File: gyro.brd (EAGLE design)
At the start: 14 x 15.2 mm, 9 parts, among them IC2 LGD20H

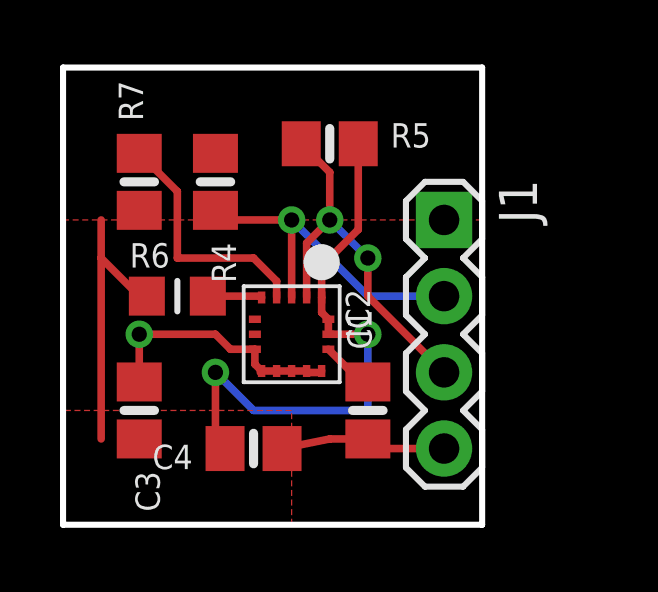
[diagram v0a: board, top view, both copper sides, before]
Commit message: boards rounted with silk screen
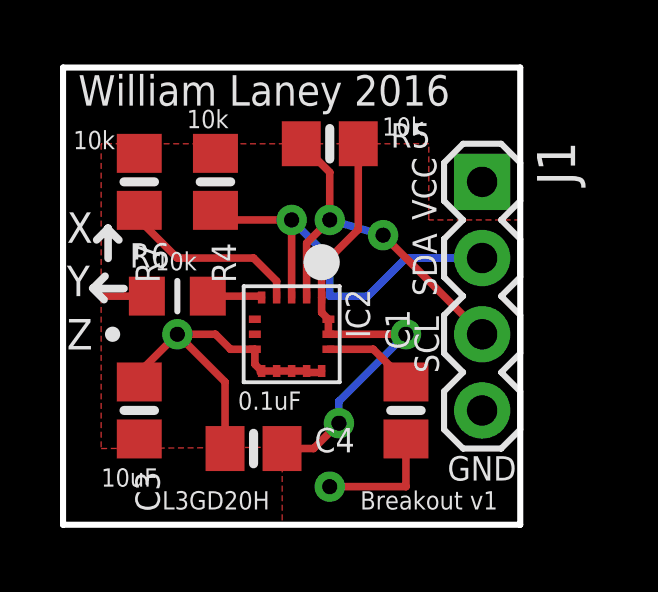
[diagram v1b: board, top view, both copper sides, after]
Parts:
- moved J1 1.80 mm to (14.0, 11.4)
- moved C1 1.27 mm to (11.4, 3.81)
- turned C4 to 0 degrees
- turned R7 to 270 degrees
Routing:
- net +3V3: track 28.4 -> 17.4 mm
- net SDA: track 11.4 -> 13.9 mm
- net GND: track 14.1 -> 16.4 mm, vias 1 -> 2
- net SDO/SAO: track 8.19 -> 6.29 mm
- net N$3: track 1.77 -> 3.04 mm
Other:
- board size 14 x 15.2 mm -> 15.2 x 15.2 mm
- board text added: "0.1uF"
- board text added: "10k"
- board text added: "10uF"
- board text added: "Breakout v1"
- board text added: "GND"
- board text added: "L3GD20H"
- board text added: "SCL"
- board text added: "SDA"
- board text added: "VCC"
- board text added: "William Laney 2016"
- board text added: "X"
- board text added: "Y"
- board text added: "Z"

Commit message: shortedn connections, removed via
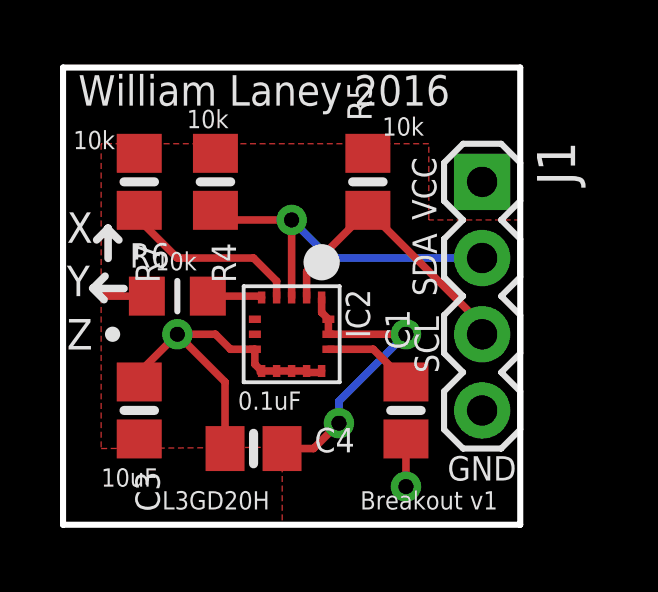
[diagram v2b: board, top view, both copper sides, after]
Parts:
- moved R5 1.80 mm to (10.2, 11.4), turned to 90 degrees
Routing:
- net +3V3: track 17.4 -> 11.8 mm
- net SCL: track 12.6 -> 9.46 mm, vias 2 -> 0
- net GND: track 16.4 -> 13.9 mm
- net SDA: track 13.9 -> 12.1 mm

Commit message: rottated header 180 degrees
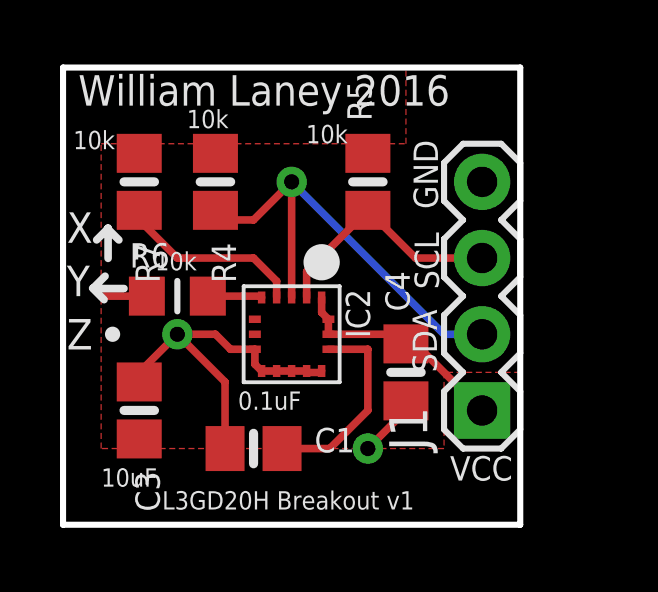
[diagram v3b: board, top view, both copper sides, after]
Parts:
- moved J1 7.62 mm to (14.0, 3.81), turned to 90 degrees
- moved C4 5.68 mm to (11.4, 5.08), turned to 90 degrees
- moved C1 5.24 mm to (6.35, 2.54), turned to 0 degrees
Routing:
- net N$3: track 3.04 -> 6.74 mm
- net SDA: track 12.1 -> 15.5 mm
- net +3V3: track 11.8 -> 9.27 mm, vias 2 -> 0
- net SCL: track 9.46 -> 8.22 mm
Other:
- board text added: "L3GD20H Breakout v1"
- board text removed: "Breakout v1"
- board text removed: "L3GD20H"
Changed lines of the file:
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@@
 <setting verticaltext="up"/>
 </settings>
-<grid distance="0.05" unitdist="inch" unit="inch" style="lines" multiple="1" display="yes" altdistance="0.005" altunitdist="inch" altunit="inch"/>
+<grid distance="0.01" unitdist="inch" unit="inch" style="lines" multiple="1" display="yes" altdistance="0.025" altunitdist="inch" altunit="inch"/>
 <layers>
 <layer number="1" name="Top" color="4" fill="1" visible="yes" active="yes"/>
@@
 <wire x1="0" y1="0" x2="15.24" y2="0" width="0.2032" layer="20"/>
 <wire x1="15.24" y1="0" x2="15.24" y2="15.24" width="0.2032" layer="20"/>
-<text x="12.446" y="10.16" size="0.8128" layer="21" ratio="15" rot="R90">VCC</text>
-<text x="15.113" y="2.286" size="0.8128" layer="21" ratio="15" rot="R180">GND</text>
-<text x="12.46281875" y="7.62" size="0.8128" layer="21" ratio="15" rot="R90">SDA</text>
-<text x="12.530521875" y="5.0574625" size="0.8128" layer="21" ratio="15" rot="R90">SCL</text>
+<text x="14.986" y="2.286" size="0.8128" layer="21" ratio="15" rot="R180">VCC</text>
+<text x="11.684" y="12.827" size="0.8128" layer="21" ratio="15" rot="R270">GND</text>
+<text x="12.46281875" y="5.08" size="0.8128" layer="21" ratio="15" rot="R90">SDA</text>
+<text x="12.530521875" y="7.8514625" size="0.8128" layer="21" ratio="15" rot="R90">SCL</text>
 <text x="1.27" y="1.27" size="0.6096" layer="21" ratio="15">10uF</text>
 <text x="5.831621875" y="3.832565625" size="0.6096" layer="21" ratio="15">0.1uF</text>
@@
 <text x="0.338071875" y="12.51946875" size="0.6096" layer="21" ratio="15">10k</text>
 <text x="0.508" y="13.97" size="1.016" layer="21">William Laney 2016</text>
-<text x="3.302" y="0.508" size="0.6096" layer="21">L3GD20H</text>
-<text x="9.906" y="0.508" size="0.6096" layer="21">Breakout v1</text>
+<text x="3.302" y="0.508" size="0.6096" layer="21">L3GD20H Breakout v1</text>
 <text x="4.124471875" y="13.2190375" size="0.6096" layer="21" ratio="15">10k</text>
-<text x="10.63798125" y="12.970803125" size="0.6096" layer="21" ratio="15">10k</text>
+<text x="8.09798125" y="12.716803125" size="0.6096" layer="21" ratio="15">10k</text>
 <text x="3.06518125" y="8.4800375" size="0.6096" layer="21" ratio="15">10k</text>
 </plain>
@@
 </autorouter>
 <elements>
-<element name="C1" library="microbuilder" package="0805-NO" value="0.1uF" x="11.43" y="3.81" rot="R90"/>
+<element name="C1" library="microbuilder" package="0805-NO" value="0.1uF" x="6.35" y="2.54"/>
 <element name="C3" library="microbuilder" package="0805-NO" value="10uF" x="2.54" y="3.81" rot="R270"/>
-<element name="C4" library="microbuilder" package="0805-NO" value="0.1uF" x="6.35" y="2.54"/>
+<element name="C4" library="microbuilder" package="0805-NO" value="0.1uF" x="11.43" y="5.08" rot="R90"/>
 <element name="IC2" library="microbuilder" package="L3GD20H_LGA16L" value="LGD20H" x="7.62" y="6.35" rot="R270"/>
 <element name="R4" library="microbuilder" package="0805-NO" value="10K" x="5.08" y="11.43" rot="R270"/>
@@
 <element name="R6" library="microbuilder" package="_0805MP" value="10K" x="3.81" y="7.62"/>
 <element name="R7" library="microbuilder" package="0805-NO" value="10K" x="2.54" y="11.43" rot="R270"/>
-<element name="J1" library="SparkFun-Connectors" package="1X04" value="" x="13.97" y="11.43" rot="R270">
-<attribute name="PROD_ID" value="CONN-09696" x="13.97" y="11.43" size="1.778" layer="27" rot="R270" display="off"/>
+<element name="J1" library="SparkFun-Connectors" package="1X04" value="" x="13.97" y="3.81" rot="R90">
+<attribute name="PROD_ID" value="CONN-09696" x="13.97" y="3.81" size="1.778" layer="27" rot="R90" display="off"/>
 </element>
 </elements>
@@
 <contactref element="C1" pad="2"/>
 <contactref element="IC2" pad="14"/>
-<wire x1="10.34" y1="5.85" x2="11.43" y2="4.76" width="0.254" layer="1"/>
-<wire x1="8.845" y1="5.85" x2="10.34" y2="5.85" width="0.254" layer="1"/>
+<wire x1="8.845" y1="5.85" x2="10.16" y2="5.85" width="0.254" layer="1"/>
+<wire x1="10.16" y1="5.85" x2="10.16" y2="3.81" width="0.254" layer="1"/>
+<wire x1="7.3" y1="2.54" x2="8.89" y2="2.54" width="0.254" layer="1"/>
+<wire x1="8.89" y1="2.54" x2="10.16" y2="3.81" width="0.254" layer="1"/>
 </signal>
 <signal name="GND">
@@
 <wire x1="8.57" y1="5.075" x2="8.17" y2="5.075" width="0.254" layer="1"/>
 <wire x1="8.17" y1="5.075" x2="8.12" y2="5.125" width="0.254" layer="1"/>
-<wire x1="6.575" y1="5.08" x2="6.62" y2="5.125" width="0.254" layer="1"/>
 <via x="3.81" y="6.35" extent="1-16" drill="0.508"/>
 <wire x1="6.395" y1="5.85" x2="6.395" y2="5.35" width="0.254" layer="1"/>
@@
 <wire x1="2.54" y1="4.76" x2="2.54" y2="5.08" width="0.254" layer="1"/>
 <wire x1="2.54" y1="5.08" x2="3.81" y2="6.35" width="0.254" layer="1"/>
-<via x="11.43" y="1.27" extent="1-16" drill="0.508"/>
+<via x="10.16" y="2.54" extent="1-16" drill="0.508"/>
+<wire x1="11.43" y1="4.13" x2="11.43" y2="3.81" width="0.254" layer="1"/>
+<wire x1="11.43" y1="3.81" x2="10.16" y2="2.54" width="0.254" layer="1"/>
 <wire x1="5.4" y1="2.54" x2="5.4" y2="4.76" width="0.254" layer="1"/>
 <wire x1="5.4" y1="4.76" x2="3.81" y2="6.35" width="0.254" layer="1"/>
-<wire x1="11.43" y1="1.27" x2="11.43" y2="2.86" width="0.254" layer="1"/>
 </signal>
 <signal name="SDO/SAO">
@@
 <wire x1="8.62" y1="7.075" x2="8.845" y2="6.85" width="0.254" layer="1"/>
 <wire x1="8.845" y1="6.85" x2="8.845" y2="6.35" width="0.254" layer="1"/>
-<via x="11.43" y="6.35" extent="1-16" drill="0.508"/>
 <wire x1="2.794" y1="7.62" x2="2.54" y2="7.62" width="0.254" layer="1"/>
-<wire x1="8.845" y1="6.35" x2="11.43" y2="6.35" width="0.254" layer="1"/>
 <wire x1="2.794" y1="7.62" x2="1.27" y2="7.62" width="0.254" layer="1"/>
-<polygon width="0.254" layer="1">
-<vertex x="15.24" y="10.16"/>
-<vertex x="12.192" y="10.16"/>
-<vertex x="12.192" y="12.7"/>
+<polygon width="0.254" layer="1" isolate="0.3048">
+<vertex x="11.43" y="12.7"/>
+<vertex x="11.43" y="15.24"/>
+<vertex x="0" y="15.24"/>
+<vertex x="0" y="0"/>
+<vertex x="15.24" y="0"/>
+<vertex x="15.24" y="5.08"/>
+<vertex x="12.7" y="5.08"/>
+<vertex x="12.7" y="2.54"/>
+<vertex x="1.27" y="2.54"/>
 <vertex x="1.27" y="12.7"/>
-<vertex x="1.27" y="2.54"/>
-<vertex x="7.304465625" y="2.58513125"/>
-<vertex x="7.304465625" y="0.04513125"/>
-<vertex x="0" y="0"/>
-<vertex x="0" y="15.24"/>
-<vertex x="15.24" y="15.24"/>
 </polygon>
-<wire x1="7.3" y1="2.54" x2="8.350540625" y2="2.54" width="0.254" layer="1"/>
-<wire x1="8.350540625" y1="2.54" x2="9.195540625" y2="3.385" width="0.254" layer="1"/>
-<via x="9.195540625" y="3.385" extent="1-16" drill="0.508"/>
-<wire x1="9.195540625" y1="3.385" x2="9.195540625" y2="4.115540625" width="0.254" layer="16"/>
-<wire x1="9.195540625" y1="4.115540625" x2="11.43" y2="6.35" width="0.254" layer="16"/>
+<wire x1="8.845" y1="6.35" x2="11.11" y2="6.35" width="0.254" layer="1"/>
+<wire x1="11.11" y1="6.35" x2="11.43" y2="6.03" width="0.254" layer="1"/>
+<wire x1="11.43" y1="6.03" x2="11.75" y2="6.03" width="0.254" layer="1"/>
+<wire x1="11.75" y1="6.03" x2="13.97" y2="3.81" width="0.254" layer="1"/>
 </signal>
 <signal name="SDA">
@@
 <contactref element="IC2" pad="3"/>
 <contactref element="J1" pad="2"/>
-<via x="7.62" y="10.16" extent="1-16" drill="0.508"/>
-<wire x1="7.62" y1="10.16" x2="7.62" y2="7.575" width="0.254" layer="1"/>
-<wire x1="7.62" y1="10.16" x2="5.4" y2="10.16" width="0.254" layer="1"/>
+<via x="7.62" y="11.43" extent="1-16" drill="0.508"/>
+<wire x1="7.62" y1="11.43" x2="7.62" y2="7.575" width="0.254" layer="1"/>
 <wire x1="5.4" y1="10.16" x2="5.08" y2="10.48" width="0.254" layer="1"/>
-<wire x1="8.89" y1="8.89" x2="7.62" y2="10.16" width="0.254" layer="16"/>
-<wire x1="13.97" y1="8.89" x2="8.89" y2="8.89" width="0.254" layer="16"/>
+<wire x1="13.97" y1="6.35" x2="12.7" y2="6.35" width="0.254" layer="16"/>
+<wire x1="12.7" y1="6.35" x2="7.62" y2="11.43" width="0.254" layer="16"/>
+<wire x1="5.4" y1="10.16" x2="6.35" y2="10.16" width="0.254" layer="1"/>
+<wire x1="6.35" y1="10.16" x2="7.62" y2="11.43" width="0.254" layer="1"/>
 </signal>
 <signal name="SCL">
@@
 <contactref element="R5" pad="1"/>
 <contactref element="J1" pad="3"/>
-<wire x1="13.97" y1="6.35" x2="13.97" y2="6.67" width="0.254" layer="1"/>
-<wire x1="13.97" y1="6.67" x2="10.16" y2="10.48" width="0.254" layer="1"/>
 <wire x1="8.12" y1="7.575" x2="8.12" y2="8.44" width="0.254" layer="1"/>
 <wire x1="8.12" y1="8.44" x2="10.16" y2="10.48" width="0.254" layer="1"/>
+<wire x1="13.97" y1="8.89" x2="11.75" y2="8.89" width="0.254" layer="1"/>
+<wire x1="11.75" y1="8.89" x2="10.16" y2="10.48" width="0.254" layer="1"/>
 </signal>
 <signal name="CS_3.3V">

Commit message: added six pin header to stack with accell
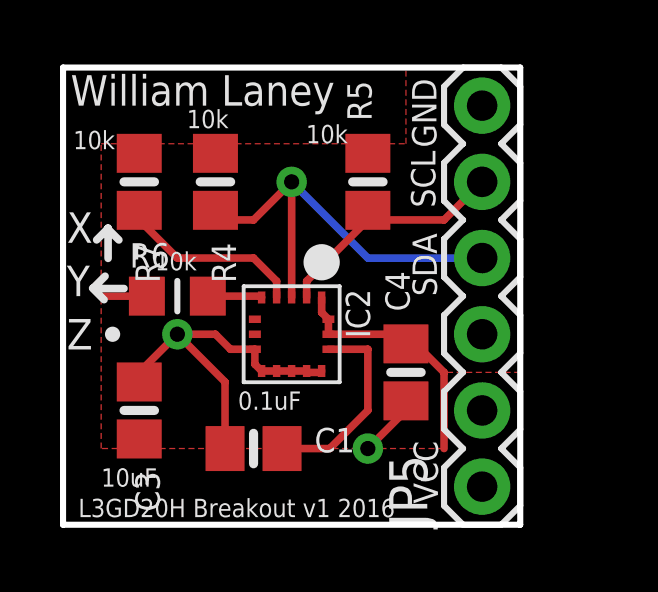
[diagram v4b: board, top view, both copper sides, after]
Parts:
- removed J1: (no value), SparkFun-Connectors:1X04
- added JP5: (no value), SparkFun:1X06
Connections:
- net +3V3: now also JP5.1; no longer J1.1
- net GND: now also JP5.6; no longer J1.4
- net SCL: now also JP5.5; no longer J1.3
- net SDA: now also JP5.4; no longer J1.2
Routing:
- net +3V3: track 9.27 -> 10.8 mm
- net SDA: track 15.5 -> 14.5 mm
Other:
- board text added: "L3GD20H Breakout v1 2016"
- board text added: "William Laney"
- board text removed: "L3GD20H Breakout v1"
- board text removed: "William Laney 2016"
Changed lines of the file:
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@@
 <wire x1="0" y1="0" x2="15.24" y2="0" width="0.2032" layer="20"/>
 <wire x1="15.24" y1="0" x2="15.24" y2="15.24" width="0.2032" layer="20"/>
-<text x="14.986" y="2.286" size="0.8128" layer="21" ratio="15" rot="R180">VCC</text>
-<text x="11.684" y="12.827" size="0.8128" layer="21" ratio="15" rot="R270">GND</text>
-<text x="12.46281875" y="5.08" size="0.8128" layer="21" ratio="15" rot="R90">SDA</text>
-<text x="12.530521875" y="7.8514625" size="0.8128" layer="21" ratio="15" rot="R90">SCL</text>
+<text x="11.684" y="2.794" size="0.8128" layer="21" ratio="15" rot="R270">VCC</text>
+<text x="12.446" y="12.573" size="0.8128" layer="21" ratio="15" rot="R90">GND</text>
+<text x="12.46281875" y="7.62" size="0.8128" layer="21" ratio="15" rot="R90">SDA</text>
+<text x="11.599478125" y="12.4685375" size="0.8128" layer="21" ratio="15" rot="R270">SCL</text>
 <text x="1.27" y="1.27" size="0.6096" layer="21" ratio="15">10uF</text>
 <text x="5.831621875" y="3.832565625" size="0.6096" layer="21" ratio="15">0.1uF</text>
@@
 <wire x1="1.50085625" y1="9.875925" x2="1.11985625" y2="9.494925" width="0.254" layer="21"/>
 <text x="0.338071875" y="12.51946875" size="0.6096" layer="21" ratio="15">10k</text>
-<text x="0.508" y="13.97" size="1.016" layer="21">William Laney 2016</text>
-<text x="3.302" y="0.508" size="0.6096" layer="21">L3GD20H Breakout v1</text>
+<text x="0.254" y="13.97" size="1.016" layer="21">William Laney</text>
+<text x="0.508" y="0.254" size="0.6096" layer="21">L3GD20H Breakout v1 2016</text>
 <text x="4.124471875" y="13.2190375" size="0.6096" layer="21" ratio="15">10k</text>
 <text x="8.09798125" y="12.716803125" size="0.6096" layer="21" ratio="15">10k</text>
@@
 <element name="R6" library="microbuilder" package="_0805MP" value="10K" x="3.81" y="7.62"/>
 <element name="R7" library="microbuilder" package="0805-NO" value="10K" x="2.54" y="11.43" rot="R270"/>
-<element name="J1" library="SparkFun-Connectors" package="1X04" value="" x="13.97" y="3.81" rot="R90">
-<attribute name="PROD_ID" value="CONN-09696" x="13.97" y="3.81" size="1.778" layer="27" rot="R90" display="off"/>
-</element>
+<element name="JP5" library="SparkFun" package="1X06" value="" x="13.97" y="1.27" rot="R90"/>
 </elements>
 <signals>
@@
 <contactref element="C3" pad="1"/>
 <contactref element="C4" pad="1"/>
-<contactref element="J1" pad="4"/>
 <wire x1="8.57" y1="5.075" x2="8.62" y2="5.125" width="0.254" layer="1"/>
 <wire x1="6.62" y1="5.125" x2="7.12" y2="5.125" width="0.254" layer="1"/>
@@
 <wire x1="5.4" y1="2.54" x2="5.4" y2="4.76" width="0.254" layer="1"/>
 <wire x1="5.4" y1="4.76" x2="3.81" y2="6.35" width="0.254" layer="1"/>
+<contactref element="JP5" pad="6"/>
 </signal>
 <signal name="SDO/SAO">
@@
 <contactref element="IC2" pad="16"/>
 <contactref element="R7" pad="1"/>
-<contactref element="J1" pad="1"/>
 <wire x1="8.62" y1="7.575" x2="8.62" y2="7.075" width="0.254" layer="1"/>
 <wire x1="8.62" y1="7.075" x2="8.845" y2="6.85" width="0.254" layer="1"/>
-<wire x1="8.845" y1="6.85" x2="8.845" y2="6.35" width="0.254" layer="1"/>
 <wire x1="2.794" y1="7.62" x2="2.54" y2="7.62" width="0.254" layer="1"/>
 <wire x1="2.794" y1="7.62" x2="1.27" y2="7.62" width="0.254" layer="1"/>
@@
 <vertex x="1.27" y="12.7"/>
 </polygon>
+<wire x1="11.43" y1="6.03" x2="11.75" y2="6.03" width="0.254" layer="1"/>
+<contactref element="JP5" pad="1"/>
+<wire x1="11.11" y1="6.35" x2="11.43" y2="6.35" width="0.254" layer="1"/>
+<wire x1="11.43" y1="6.35" x2="12.7" y2="5.08" width="0.254" layer="1"/>
+<wire x1="12.7" y1="5.08" x2="12.7" y2="2.54" width="0.254" layer="1"/>
 <wire x1="8.845" y1="6.35" x2="11.11" y2="6.35" width="0.254" layer="1"/>
 <wire x1="11.11" y1="6.35" x2="11.43" y2="6.03" width="0.254" layer="1"/>
-<wire x1="11.43" y1="6.03" x2="11.75" y2="6.03" width="0.254" layer="1"/>
-<wire x1="11.75" y1="6.03" x2="13.97" y2="3.81" width="0.254" layer="1"/>
+<wire x1="8.845" y1="6.35" x2="8.845" y2="6.85" width="0.254" layer="1"/>
 </signal>
 <signal name="SDA">
 <contactref element="R4" pad="2"/>
 <contactref element="IC2" pad="3"/>
-<contactref element="J1" pad="2"/>
 <via x="7.62" y="11.43" extent="1-16" drill="0.508"/>
 <wire x1="7.62" y1="11.43" x2="7.62" y2="7.575" width="0.254" layer="1"/>
 <wire x1="5.4" y1="10.16" x2="5.08" y2="10.48" width="0.254" layer="1"/>
-<wire x1="13.97" y1="6.35" x2="12.7" y2="6.35" width="0.254" layer="16"/>
-<wire x1="12.7" y1="6.35" x2="7.62" y2="11.43" width="0.254" layer="16"/>
 <wire x1="5.4" y1="10.16" x2="6.35" y2="10.16" width="0.254" layer="1"/>
 <wire x1="6.35" y1="10.16" x2="7.62" y2="11.43" width="0.254" layer="1"/>
+<contactref element="JP5" pad="4"/>
+<wire x1="13.97" y1="8.89" x2="10.16" y2="8.89" width="0.254" layer="16"/>
+<wire x1="10.16" y1="8.89" x2="7.62" y2="11.43" width="0.254" layer="16"/>
 </signal>
 <signal name="SCL">
 <contactref element="IC2" pad="2"/>
 <contactref element="R5" pad="1"/>
-<contactref element="J1" pad="3"/>
-<wire x1="8.12" y1="7.575" x2="8.12" y2="8.44" width="0.254" layer="1"/>
-<wire x1="8.12" y1="8.44" x2="10.16" y2="10.48" width="0.254" layer="1"/>
-<wire x1="13.97" y1="8.89" x2="11.75" y2="8.89" width="0.254" layer="1"/>
-<wire x1="11.75" y1="8.89" x2="10.16" y2="10.48" width="0.254" layer="1"/>
+<contactref element="JP5" pad="5"/>
+<wire x1="10.16" y1="10.16" x2="12.7" y2="10.16" width="0.254" layer="1"/>
+<wire x1="12.7" y1="10.16" x2="13.97" y2="11.43" width="0.254" layer="1"/>
+<wire x1="10.16" y1="10.16" x2="8.12" y2="8.12" width="0.254" layer="1"/>
+<wire x1="8.12" y1="7.575" x2="8.12" y2="8.12" width="0.254" layer="1"/>
+<wire x1="10.16" y1="10.16" x2="10.16" y2="10.48" width="0.254" layer="1"/>
 </signal>
 <signal name="CS_3.3V">
